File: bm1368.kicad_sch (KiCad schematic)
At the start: 49 parts, among them U5 MCP1824T-1202E/OT, U6 MCP1824T-0802E, U7 25MHz, U8 BM1368_mode1, U9 SN74AVC4T774

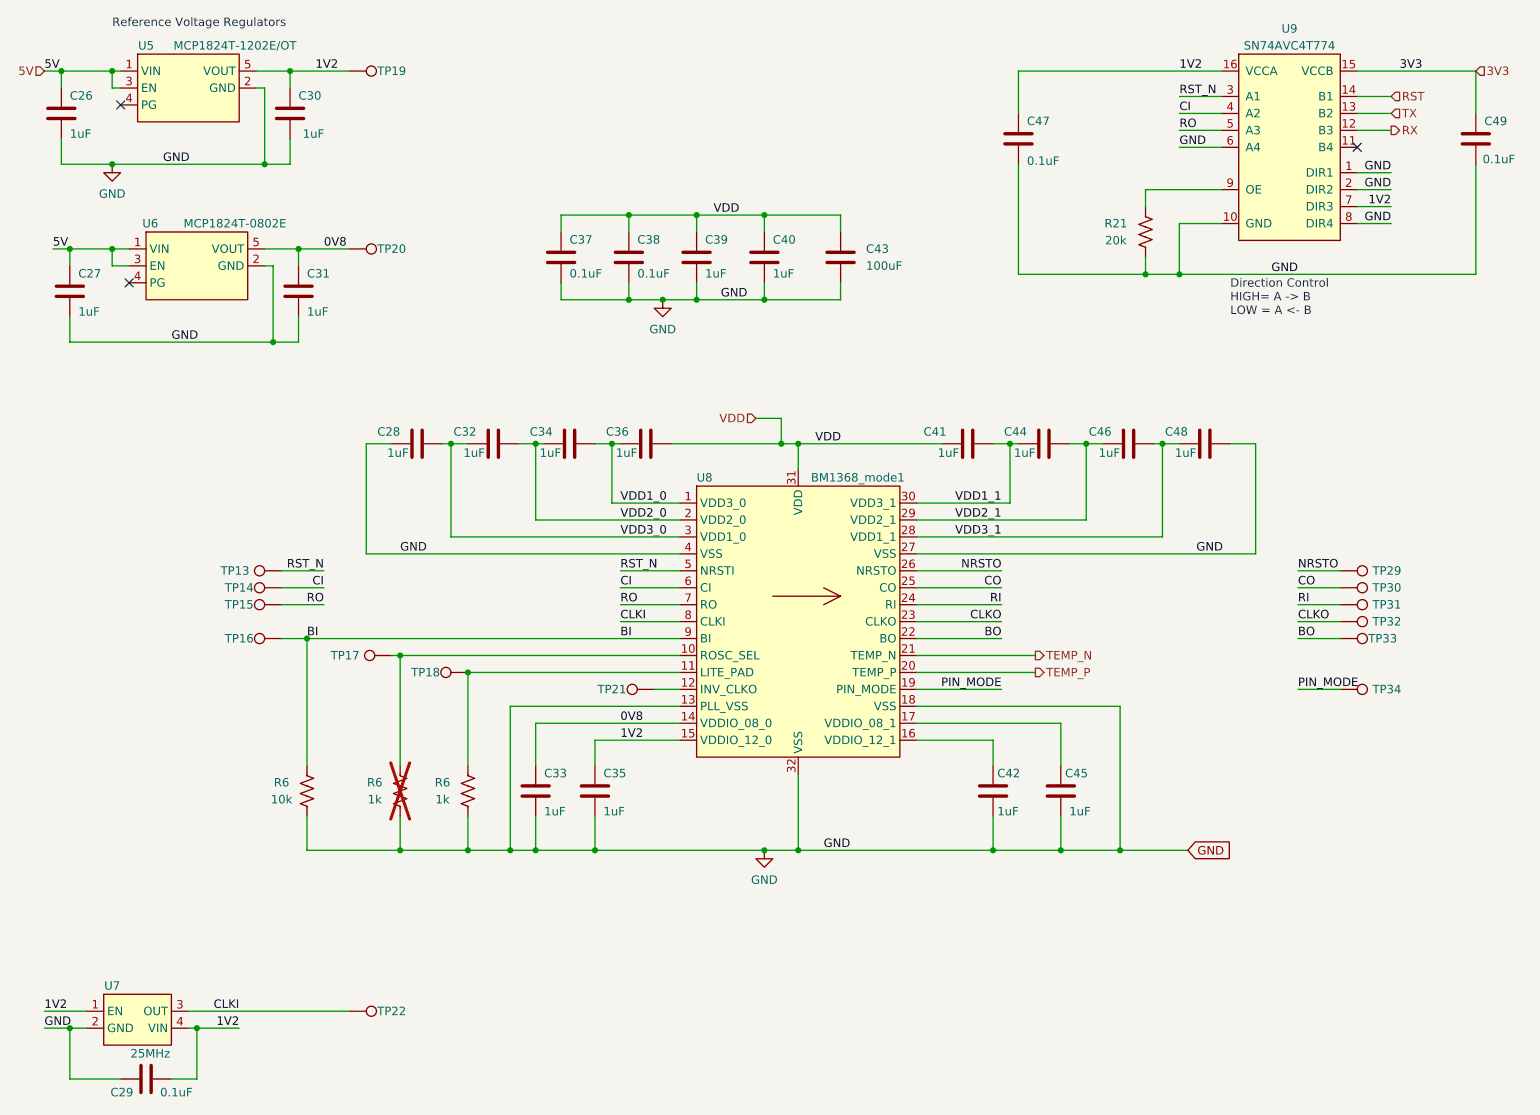
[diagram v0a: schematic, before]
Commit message: Add BitcoinMerch Logo
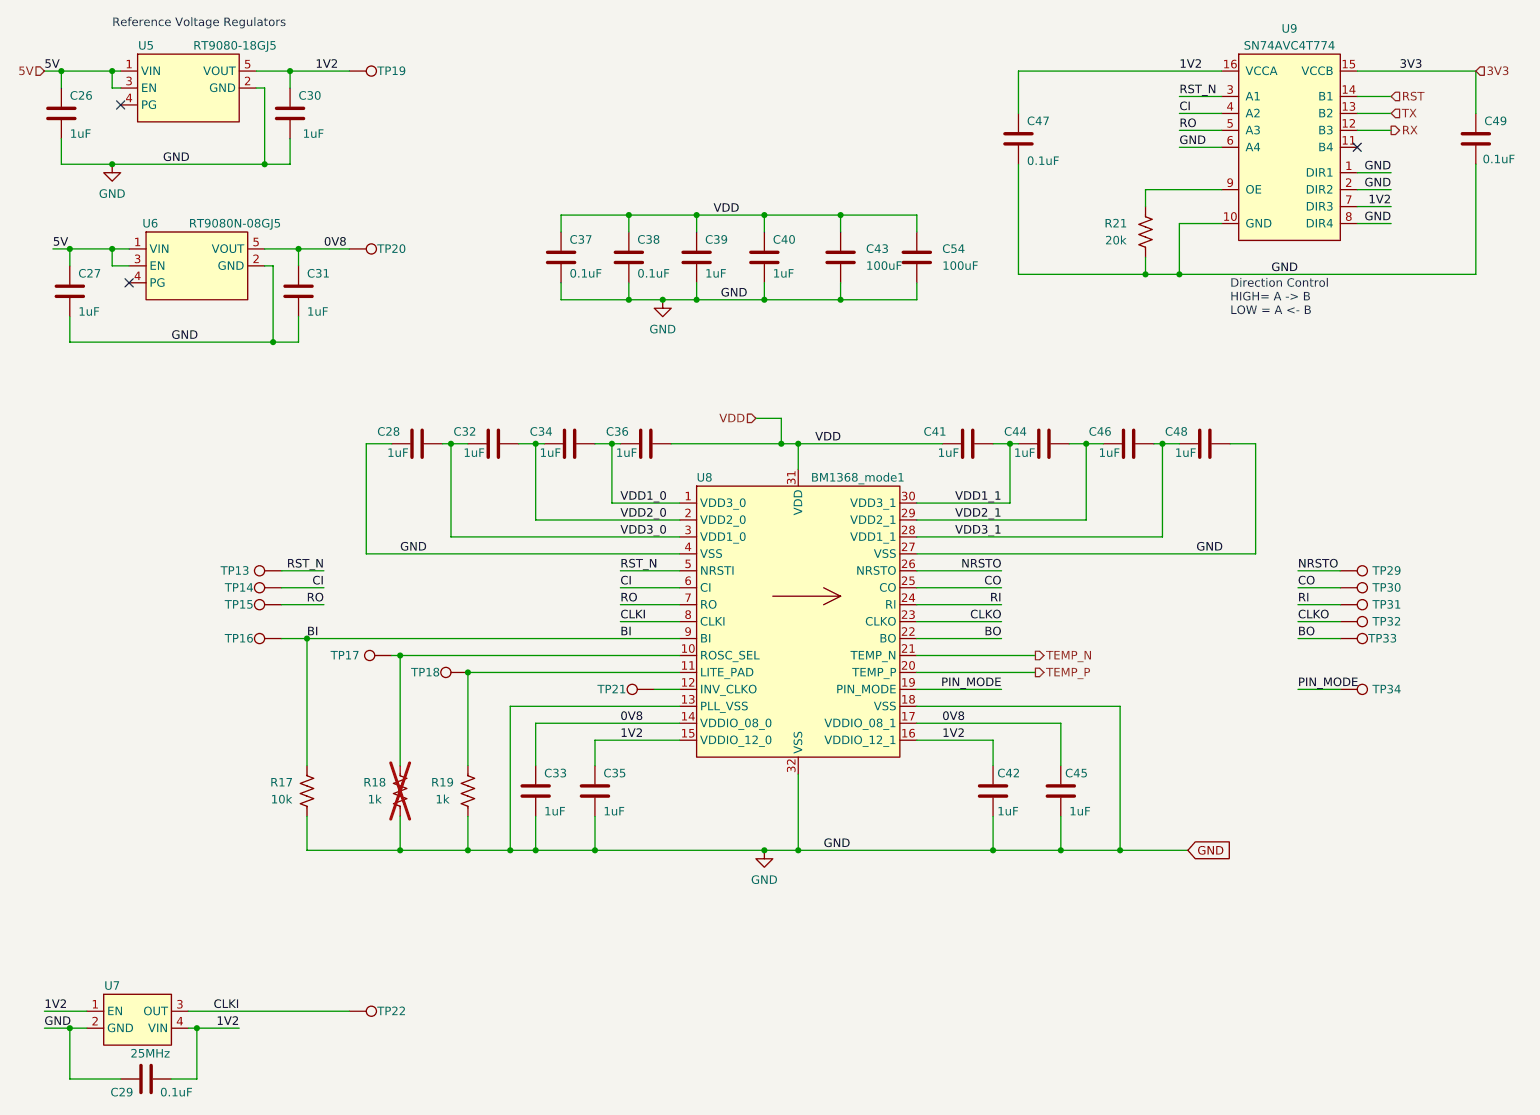
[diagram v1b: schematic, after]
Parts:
- added C54: 100uF, Capacitor_SMD:C_1206_3216Metric, symbol Device:C
- U5: value MCP1824T-1202E/OT -> RT9080-18GJ5
- U6: value MCP1824T-0802E -> RT9080N-08GJ5
- renumbered R6 to R17, R6 to R18, R6 to R19
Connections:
- net 0V8: now also C45.1, U8.17 (VDDIO_08_1)
- net 1V2: now also C42.1, U8.16 (VDDIO_12_1)
- net GND: now also C54.2
- net VDD: now also C54.1
